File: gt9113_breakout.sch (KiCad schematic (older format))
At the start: 9 parts, among them J1 Conn_01x04_Male, J2 10118194-0001LF, J7 504740-5100, J8 504740-5100, U2 HT7533-1-SOT89

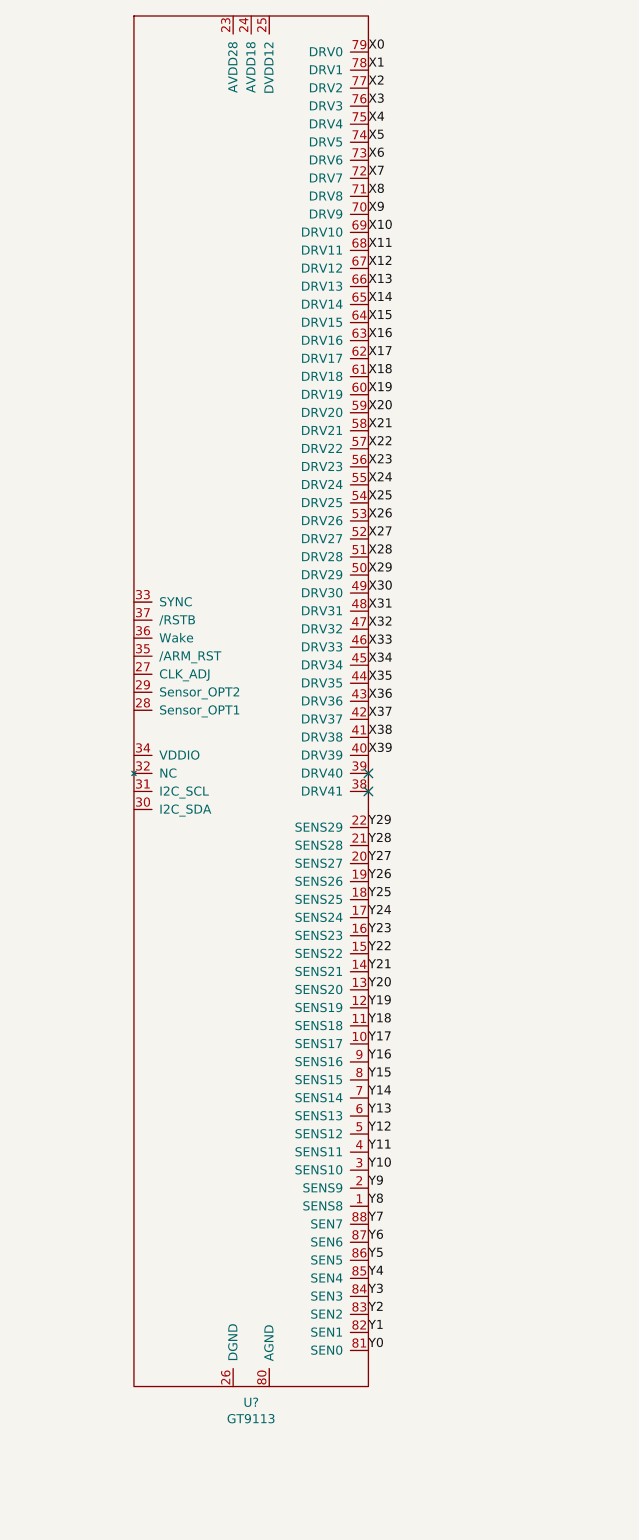
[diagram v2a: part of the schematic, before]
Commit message: Add footprint for GT9113. Start to route the drive/sense pins.
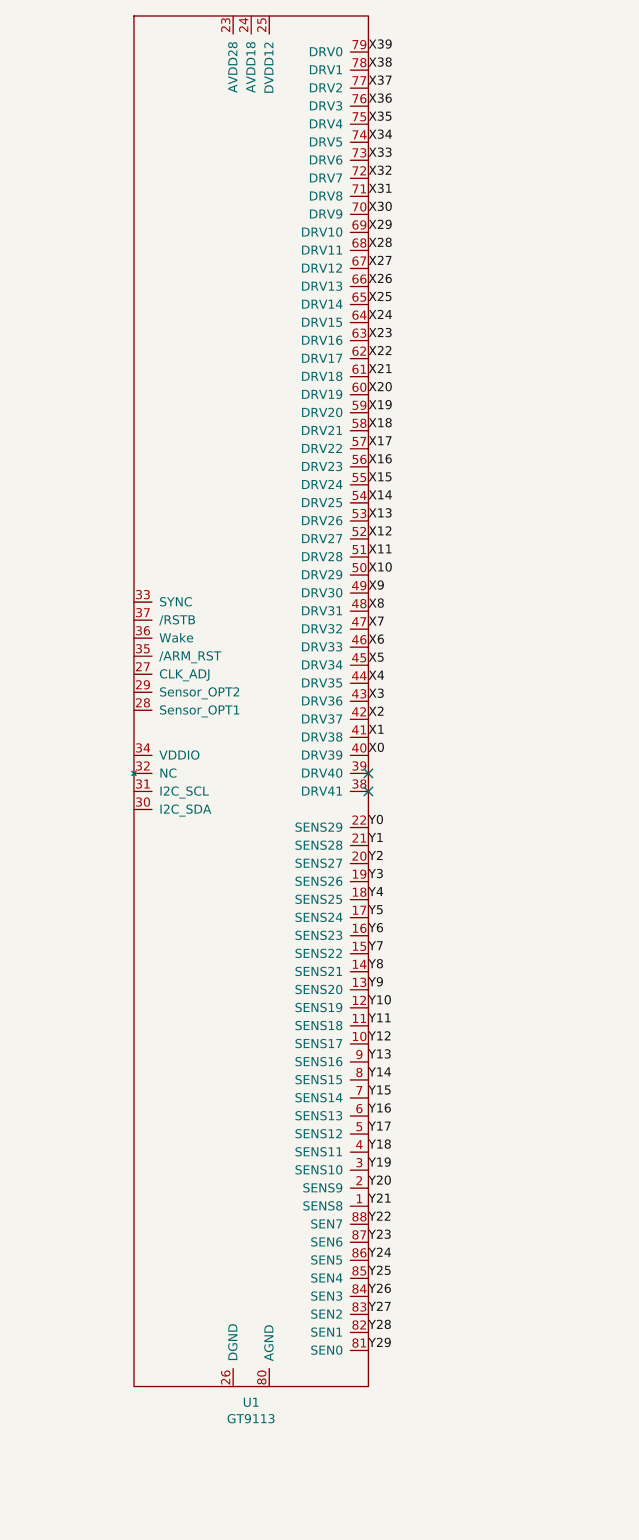
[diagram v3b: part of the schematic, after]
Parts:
- U1: renamed from U?; footprint (none) -> footprints:GT9113
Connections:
- net X0: now also U1.40 (DRV39); no longer U1.79 (DRV0)
- net X1: now also U1.41 (DRV38); no longer U1.78 (DRV1)
- net X10: now also U1.50 (DRV29); no longer U1.69 (DRV10)
- net X11: now also U1.51 (DRV28); no longer U1.68 (DRV11)
- net X12: now also U1.52 (DRV27); no longer U1.67 (DRV12)
- net X13: now also U1.53 (DRV26); no longer U1.66 (DRV13)
- net X14: now also U1.54 (DRV25); no longer U1.65 (DRV14)
- net X15: now also U1.55 (DRV24); no longer U1.64 (DRV15)
- net X16: now also U1.56 (DRV23); no longer U1.63 (DRV16)
- net X17: now also U1.57 (DRV22); no longer U1.62 (DRV17)
- net X18: now also U1.58 (DRV21); no longer U1.61 (DRV18)
- net X19: now also U1.59 (DRV20); no longer U1.60 (DRV19)
- net X2: now also U1.42 (DRV37); no longer U1.77 (DRV2)
- net X20: now also U1.60 (DRV19); no longer U1.59 (DRV20)
- net X21: now also U1.61 (DRV18); no longer U1.58 (DRV21)
- net X22: now also U1.62 (DRV17); no longer U1.57 (DRV22)
- net X23: now also U1.63 (DRV16); no longer U1.56 (DRV23)
- net X24: now also U1.64 (DRV15); no longer U1.55 (DRV24)
- net X25: now also U1.65 (DRV14); no longer U1.54 (DRV25)
- net X26: now also U1.66 (DRV13); no longer U1.53 (DRV26)
- net X27: now also U1.67 (DRV12); no longer U1.52 (DRV27)
- net X28: now also U1.68 (DRV11); no longer U1.51 (DRV28)
- net X29: now also U1.69 (DRV10); no longer U1.50 (DRV29)
- net X3: now also U1.43 (DRV36); no longer U1.76 (DRV3)
- net X30: now also U1.70 (DRV9); no longer U1.49 (DRV30)
- net X31: now also U1.71 (DRV8); no longer U1.48 (DRV31)
- net X32: now also U1.72 (DRV7); no longer U1.47 (DRV32)
- net X33: now also U1.73 (DRV6); no longer U1.46 (DRV33)
- net X34: now also U1.74 (DRV5); no longer U1.45 (DRV34)
- net X35: now also U1.75 (DRV4); no longer U1.44 (DRV35)
- net X36: now also U1.76 (DRV3); no longer U1.43 (DRV36)
- net X37: now also U1.77 (DRV2); no longer U1.42 (DRV37)
- net X38: now also U1.78 (DRV1); no longer U1.41 (DRV38)
- net X39: now also U1.79 (DRV0); no longer U1.40 (DRV39)
- net X4: now also U1.44 (DRV35); no longer U1.75 (DRV4)
- net X5: now also U1.45 (DRV34); no longer U1.74 (DRV5)
- net X6: now also U1.46 (DRV33); no longer U1.73 (DRV6)
- net X7: now also U1.47 (DRV32); no longer U1.72 (DRV7)
- net X8: now also U1.48 (DRV31); no longer U1.71 (DRV8)
- net X9: now also U1.49 (DRV30); no longer U1.70 (DRV9)
- net Y0: now also U1.22 (SENS29); no longer U1.81 (SEN0)
- net Y1: now also U1.21 (SENS28); no longer U1.82 (SEN1)
- net Y10: now also U1.12 (SENS19); no longer U1.3 (SENS10)
- net Y11: now also U1.11 (SENS18); no longer U1.4 (SENS11)
- net Y12: now also U1.10 (SENS17); no longer U1.5 (SENS12)
- net Y13: now also U1.9 (SENS16); no longer U1.6 (SENS13)
- net Y14: now also U1.8 (SENS15); no longer U1.7 (SENS14)
- net Y15: now also U1.7 (SENS14); no longer U1.8 (SENS15)
- net Y16: now also U1.6 (SENS13); no longer U1.9 (SENS16)
- net Y17: now also U1.5 (SENS12); no longer U1.10 (SENS17)
- net Y18: now also U1.4 (SENS11); no longer U1.11 (SENS18)
- net Y19: now also U1.3 (SENS10); no longer U1.12 (SENS19)
- net Y2: now also U1.20 (SENS27); no longer U1.83 (SEN2)
- net Y20: now also U1.2 (SENS9); no longer U1.13 (SENS20)
- net Y21: now also U1.1 (SENS8); no longer U1.14 (SENS21)
- net Y22: now also U1.88 (SEN7); no longer U1.15 (SENS22)
- net Y23: now also U1.87 (SEN6); no longer U1.16 (SENS23)
- net Y24: now also U1.86 (SEN5); no longer U1.17 (SENS24)
- net Y25: now also U1.85 (SEN4); no longer U1.18 (SENS25)
- net Y26: now also U1.84 (SEN3); no longer U1.19 (SENS26)
- net Y27: now also U1.83 (SEN2); no longer U1.20 (SENS27)
- net Y28: now also U1.82 (SEN1); no longer U1.21 (SENS28)
- net Y29: now also U1.81 (SEN0); no longer U1.22 (SENS29)
- net Y3: now also U1.19 (SENS26); no longer U1.84 (SEN3)
- net Y4: now also U1.18 (SENS25); no longer U1.85 (SEN4)
- net Y5: now also U1.17 (SENS24); no longer U1.86 (SEN5)
- net Y6: now also U1.16 (SENS23); no longer U1.87 (SEN6)
- net Y7: now also U1.15 (SENS22); no longer U1.88 (SEN7)
- net Y8: now also U1.14 (SENS21); no longer U1.1 (SENS8)
- net Y9: now also U1.13 (SENS20); no longer U1.2 (SENS9)
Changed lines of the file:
@@
 VIN_3.3
 $Comp
-L gt9113:GT9113 U?
+L gt9113:GT9113 U1
 U 1 1 60371774
 P 9850 5550
-F 0 "U?" H 9850 1661 50  0000 C CNN
+F 0 "U1" H 9850 1661 50  0000 C CNN
 F 1 "GT9113" H 9850 1570 50  0000 C CNN
-F 2 "" H 9800 6100 50  0001 C CNN
+F 2 "footprints:GT9113" H 9800 6100 50  0001 C CNN
 F 3 "" H 9800 6100 50  0001 C CNN
 	1    9850 5550
 	1    0    0    -1
 $EndComp
+Text Label 10500 5850 0    50   ~ 0
+X0
+Text Label 10500 5750 0    50   ~ 0
+X1
+Text Label 10500 5650 0    50   ~ 0
+X2
+Text Label 10500 5550 0    50   ~ 0
+X3
+Text Label 10500 5450 0    50   ~ 0
+X4
+Text Label 10500 5350 0    50   ~ 0
+X5
+Text Label 10500 5250 0    50   ~ 0
+X6
+Text Label 10500 5150 0    50   ~ 0
+X7
+Text Label 10500 5050 0    50   ~ 0
+X8
+Text Label 10500 4950 0    50   ~ 0
+X9
+Text Label 10500 4850 0    50   ~ 0
+X10
+Text Label 10500 4750 0    50   ~ 0
+X11
+Text Label 10500 4650 0    50   ~ 0
+X12
+Text Label 10500 4550 0    50   ~ 0
+X13
+Text Label 10500 4450 0    50   ~ 0
+X14
+Text Label 10500 4350 0    50   ~ 0
+X15
+Text Label 10500 4250 0    50   ~ 0
+X16
+Text Label 10500 4150 0    50   ~ 0
+X17
+Text Label 10500 4050 0    50   ~ 0
+X18
+Text Label 10500 3950 0    50   ~ 0
+X19
+Text Label 10500 3850 0    50   ~ 0
+X20
+Text Label 10500 3750 0    50   ~ 0
+X21
+Text Label 10500 3650 0    50   ~ 0
+X22
+Text Label 10500 3550 0    50   ~ 0
+X23
+Text Label 10500 3450 0    50   ~ 0
+X24
+Text Label 10500 3350 0    50   ~ 0
+X25
+Text Label 10500 3250 0    50   ~ 0
+X26
+Text Label 10500 3150 0    50   ~ 0
+X27
+Text Label 10500 3050 0    50   ~ 0
+X28
+Text Label 10500 2950 0    50   ~ 0
+X29
+Text Label 10500 2850 0    50   ~ 0
+X30
+Text Label 10500 2750 0    50   ~ 0
+X31
+Text Label 10500 2650 0    50   ~ 0
+X32
+Text Label 10500 2550 0    50   ~ 0
+X33
+Text Label 10500 2450 0    50   ~ 0
+X34
+Text Label 10500 2350 0    50   ~ 0
+X35
+Text Label 10500 2250 0    50   ~ 0
+X36
+Text Label 10500 2150 0    50   ~ 0
+X37
+Text Label 10500 2050 0    50   ~ 0
+X38
 Text Label 10500 1950 0    50   ~ 0
-X0
-Text Label 10500 2050 0    50   ~ 0
-X1
-Text Label 10500 2150 0    50   ~ 0
-X2
-Text Label 10500 2250 0    50   ~ 0
-X3
-Text Label 10500 2350 0    50   ~ 0
-X4
-Text Label 10500 2450 0    50   ~ 0
-X5
-Text Label 10500 2550 0    50   ~ 0
-X6
-Text Label 10500 2650 0    50   ~ 0
-X7
-Text Label 10500 2750 0    50   ~ 0
-X8
-Text Label 10500 2850 0    50   ~ 0
-X9
-Text Label 10500 2950 0    50   ~ 0
-X10
-Text Label 10500 3050 0    50   ~ 0
-X11
-Text Label 10500 3150 0    50   ~ 0
-X12
-Text Label 10500 3250 0    50   ~ 0
-X13
-Text Label 10500 3350 0    50   ~ 0
-X14
-Text Label 10500 3450 0    50   ~ 0
-X15
-Text Label 10500 3550 0    50   ~ 0
-X16
-Text Label 10500 3650 0    50   ~ 0
-X17
-Text Label 10500 3750 0    50   ~ 0
-X18
-Text Label 10500 3850 0    50   ~ 0
-X19
-Text Label 10500 3950 0    50   ~ 0
-X20
-Text Label 10500 4050 0    50   ~ 0
-X21
-Text Label 10500 4150 0    50   ~ 0
-X22
-Text Label 10500 4250 0    50   ~ 0
-X23
-Text Label 10500 4350 0    50   ~ 0
-X24
-Text Label 10500 4450 0    50   ~ 0
-X25
-Text Label 10500 4550 0    50   ~ 0
-X26
-Text Label 10500 4650 0    50   ~ 0
-X27
-Text Label 10500 4750 0    50   ~ 0
-X28
-Text Label 10500 4850 0    50   ~ 0
-X29
-Text Label 10500 4950 0    50   ~ 0
-X30
-Text Label 10500 5050 0    50   ~ 0
-X31
-Text Label 10500 5150 0    50   ~ 0
-X32
-Text Label 10500 5250 0    50   ~ 0
-X33
-Text Label 10500 5350 0    50   ~ 0
-X34
-Text Label 10500 5450 0    50   ~ 0
-X35
-Text Label 10500 5550 0    50   ~ 0
-X36
-Text Label 10500 5650 0    50   ~ 0
-X37
-Text Label 10500 5750 0    50   ~ 0
-X38
-Text Label 10500 5850 0    50   ~ 0
 X39
 NoConn ~ 10500 5950
 NoConn ~ 10500 6050
+Text Label 10500 6250 0    50   ~ 0
+Y0
+Text Label 10500 6350 0    50   ~ 0
+Y1
+Text Label 10500 6450 0    50   ~ 0
+Y2
+Text Label 10500 6550 0    50   ~ 0
+Y3
+Text Label 10500 6650 0    50   ~ 0
+Y4
+Text Label 10500 6750 0    50   ~ 0
+Y5
+Text Label 10500 6850 0    50   ~ 0
+Y6
+Text Label 10500 6950 0    50   ~ 0
+Y7
+Text Label 10500 7050 0    50   ~ 0
+Y8
+Text Label 10500 7150 0    50   ~ 0
+Y9
+Text Label 10500 7250 0    50   ~ 0
+Y10
+Text Label 10500 7350 0    50   ~ 0
+Y11
+Text Label 10500 7450 0    50   ~ 0
+Y12
+Text Label 10500 7550 0    50   ~ 0
+Y13
+Text Label 10500 7650 0    50   ~ 0
+Y14
+Text Label 10500 7750 0    50   ~ 0
+Y15
+Text Label 10500 7850 0    50   ~ 0
+Y16
+Text Label 10500 7950 0    50   ~ 0
+Y17
+Text Label 10500 8050 0    50   ~ 0
+Y18
+Text Label 10500 8150 0    50   ~ 0
+Y19
+Text Label 10500 8250 0    50   ~ 0
+Y20
+Text Label 10500 8350 0    50   ~ 0
+Y21
+Text Label 10500 8450 0    50   ~ 0
+Y22
+Text Label 10500 8550 0    50   ~ 0
+Y23
+Text Label 10500 8650 0    50   ~ 0
+Y24
+Text Label 10500 8750 0    50   ~ 0
+Y25
+Text Label 10500 8850 0    50   ~ 0
+Y26
+Text Label 10500 8950 0    50   ~ 0
+Y27
+Text Label 10500 9050 0    50   ~ 0
+Y28
 Text Label 10500 9150 0    50   ~ 0
-Y0
-Text Label 10500 9050 0    50   ~ 0
-Y1
-Text Label 10500 8950 0    50   ~ 0
-Y2
-Text Label 10500 8850 0    50   ~ 0
-Y3
-Text Label 10500 8750 0    50   ~ 0
-Y4
-Text Label 10500 8650 0    50   ~ 0
-Y5
-Text Label 10500 8550 0    50   ~ 0
-Y6
-Text Label 10500 8450 0    50   ~ 0
-Y7
-Text Label 10500 8350 0    50   ~ 0
-Y8
-Text Label 10500 8250 0    50   ~ 0
-Y9
-Text Label 10500 8150 0    50   ~ 0
-Y10
-Text Label 10500 8050 0    50   ~ 0
-Y11
-Text Label 10500 7950 0    50   ~ 0
-Y12
-Text Label 10500 7850 0    50   ~ 0
-Y13
-Text Label 10500 7750 0    50   ~ 0
-Y14
-Text Label 10500 7650 0    50   ~ 0
-Y15
-Text Label 10500 7550 0    50   ~ 0
-Y16
-Text Label 10500 7450 0    50   ~ 0
-Y17
-Text Label 10500 7350 0    50   ~ 0
-Y18
-Text Label 10500 7250 0    50   ~ 0
-Y19
-Text Label 10500 7150 0    50   ~ 0
-Y20
-Text Label 10500 7050 0    50   ~ 0
-Y21
-Text Label 10500 6950 0    50   ~ 0
-Y22
-Text Label 10500 6850 0    50   ~ 0
-Y23
-Text Label 10500 6750 0    50   ~ 0
-Y24
-Text Label 10500 6650 0    50   ~ 0
-Y25
-Text Label 10500 6550 0    50   ~ 0
-Y26
-Text Label 10500 6450 0    50   ~ 0
-Y27
-Text Label 10500 6350 0    50   ~ 0
-Y28
-Text Label 10500 6250 0    50   ~ 0
 Y29
 $EndSCHEMATC

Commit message: Fix up USB connector footprint so I don't have to ignore DRC errors. Add courtyard for gt9113 footprint. Wire up digital IO pins to 2.54mm header. Tweak X/Y traces.
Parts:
- removed J2: 10118194-0001LF, usb port:10118194-0001LF, symbol 10118194-0001LF:10118194-0001LF
- removed R10, R11, R12: 0, Resistor_SMD:R_0402_1005Metric, symbol Device:R
- removed U2: HT7533-1-SOT89, Package_TO_SOT_SMD:SOT-89-3, symbol Regulator_Linear:HT75xx-1-SOT89
- added C1, C2, C3: 2.2uF, Capacitor_SMD:C_0402_1005Metric, symbol Device:C
- added R1, R2: 0R/DNF, Resistor_SMD:R_0402_1005Metric, symbol Device:R
- added R3: 300k/DNF, Resistor_SMD:R_0402_1005Metric, symbol Device:R
- J1: value Conn_01x04_Male -> Conn_01x09_Male; footprint Connector_PinHeader_2.54mm:PinHeader_1x06_P2.54mm_Vertical -> Connector_PinHeader_2.54mm:PinHeader_1x09_P2.54mm_Vertical; symbol Connector:Conn_01x06_Male -> Connector:Conn_01x09_Male
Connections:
- net ~CHG is gone; now on net VIN_3.3: J1.6 (Pin_6)
- net ~RESET is gone; now on net SYNC: J1.5 (Pin_5)
- net GND: now also J1.4 (Pin_4), U1.26 (DGND), U1.80 (AGND), C1.2, C2.2, C3.2, R2.1, R3.1; no longer J1.1 (Pin_1)
- net SCL: now also J1.3 (Pin_3), U1.31 (I2C_SCL); no longer J1.4 (Pin_4)
- net SDA: now also J1.2 (Pin_2), U1.30 (I2C_SDA); no longer J1.3 (Pin_3)
- net VIN_3.3: now also U1.34 (VDDIO), R1.2; no longer J1.2 (Pin_2)
- net at U1.23 (AVDD28): now also C3.1
- net at U1.24 (AVDD18): now also C2.1
- net at U1.25 (DVDD12): now also C1.1
- net CLK_ADJ: now reaches U1.27 (CLK_ADJ)
- net CLK_ADJ: now also J1.1 (Pin_1)
- net at U1.28 (Sensor_OPT1): now also R3.2
- net at U1.29 (Sensor_OPT2): now also R1.1, R2.2
- net SYNC: now reaches U1.33 (SYNC)
- net ARM_RST: now reaches U1.35 (/ARM_RST)
- net ARM_RST: now also J1.7 (Pin_7)
- net Wake: now reaches U1.36 (Wake)
- net Wake: now also J1.8 (Pin_8)
- net RSTB: now reaches U1.37 (/RSTB)
- net RSTB: now also J1.9 (Pin_9)
- no-connect marks 3 -> 2
